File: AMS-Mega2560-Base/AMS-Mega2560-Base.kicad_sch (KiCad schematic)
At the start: 29 parts, among them J1 Conn_01x03, J2 Conn_01x03, J3 Conn_01x08, J4 Sense1, J5 Sense2, J6 AdafruitUltimateGPS, J7 Conn_02x03_Odd_Even, J8 Conn_01x03, P1 Power, P10 CONN_01X01, P11 CONN_01X01, P12 CONN_01X01, P13 CONN_01X01, P2 Analog, P3 Analog, P4 Digital, P5 PWM, P6 PWM, P7 Communication, P8 CONN_01X01, P9 CONN_01X01, T1 Conn_01x08, T2 Conn_01x08, T3 Conn_01x08, T4 Conn_01x08, T5 Conn_01x08, T6 Conn_01x08

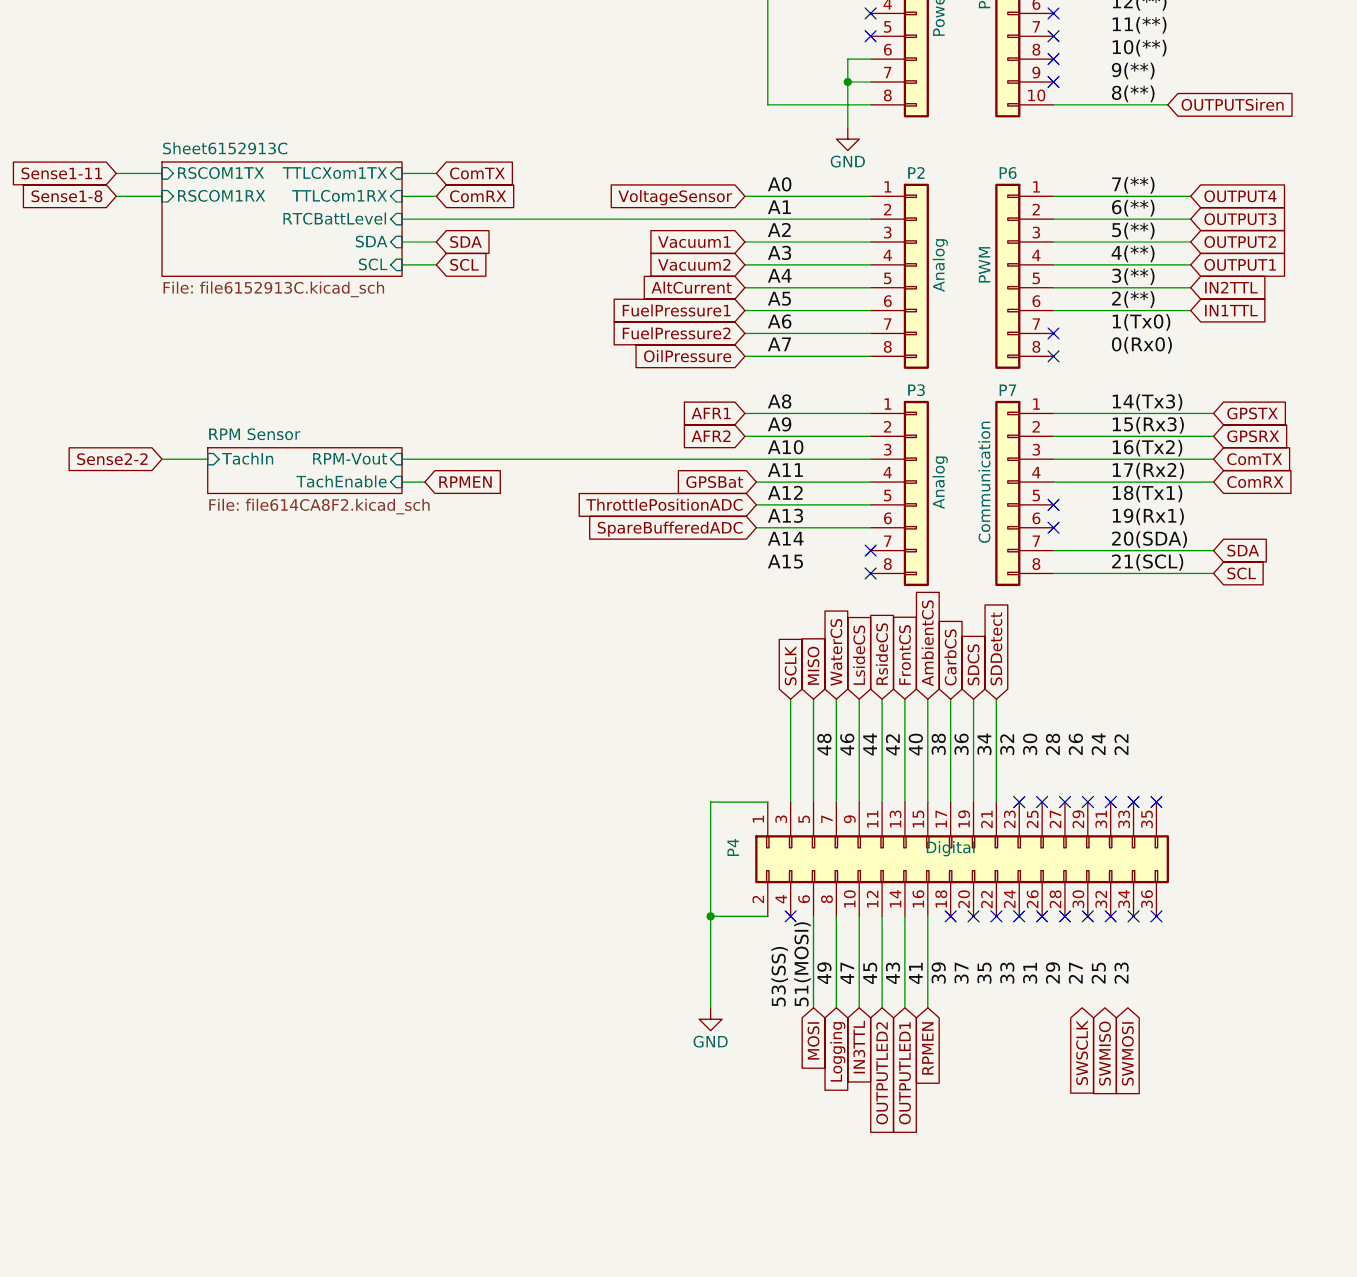
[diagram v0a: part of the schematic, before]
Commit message: working on fixing the screw ups. adding a second serial port
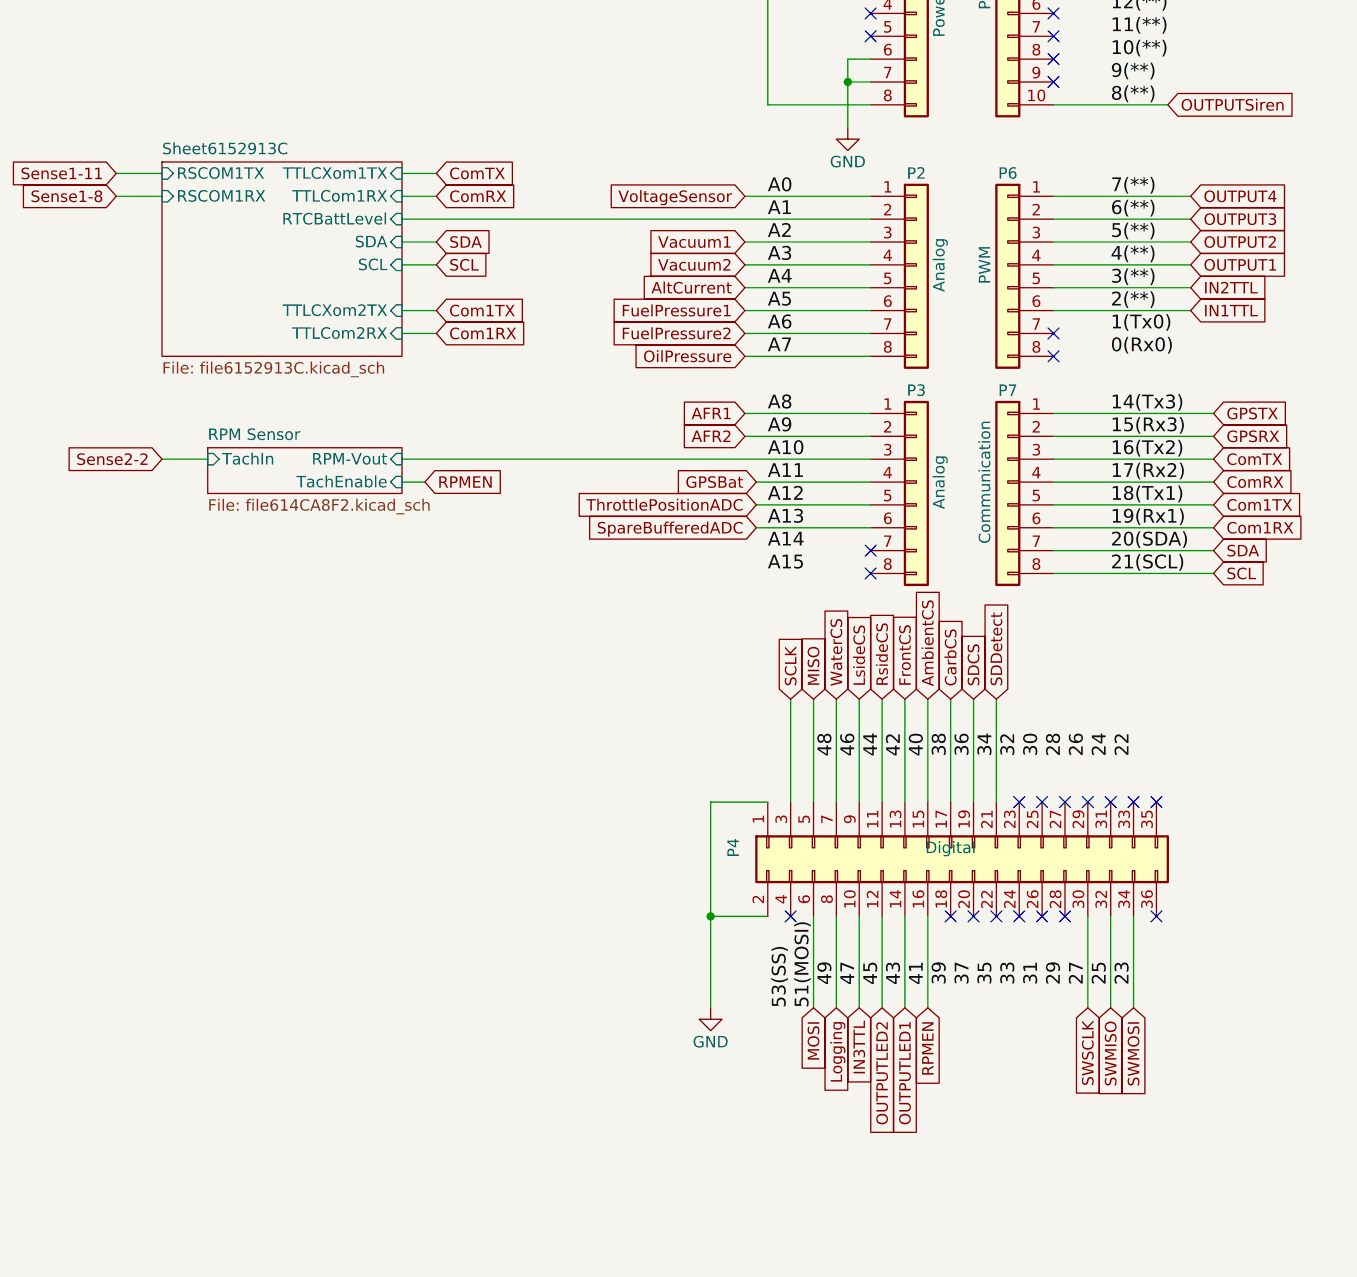
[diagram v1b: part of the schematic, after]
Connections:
- net SWMISO: now also P4.32 (Pin_32)
- net SWMOSI: now also P4.34 (Pin_34)
- net SWSCLK: now also P4.30 (Pin_30)
- net Com1TX: now reaches P7.5 (Pin_5)
- net Com1RX: now reaches P7.6 (Pin_6)
- no-connect marks 58 -> 53
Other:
- sheet Sheet6152913C ports: added TTLCXom2TX, TTLCom2RX; removed none
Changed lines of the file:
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@@
   (no_connect (at 61.595 233.045))
   (no_connect (at 355.6 101.6))
-  (no_connect (at 375.92 96.52))
-  (no_connect (at 375.92 99.06))
   (no_connect (at 364.49 142.24))
   (no_connect (at 367.03 142.24))
@@
   (no_connect (at 372.11 142.24))
   (no_connect (at 374.65 142.24))
-  (no_connect (at 382.27 142.24))
-  (no_connect (at 384.81 142.24))
   (no_connect (at 377.19 142.24))
-  (no_connect (at 379.73 142.24))
   (no_connect (at 369.57 142.24))
   (no_connect (at 375.92 49.53))
@@
     (stroke (width 0) (type default) (color 0 0 0 0))
   )
+  (wire (pts (xy 303.53 74.93) (xy 307.34 74.93))
+    (stroke (width 0) (type default) (color 0 0 0 0))
+  )
   (wire (pts (xy 367.03 118.11) (xy 367.03 129.54))
     (stroke (width 0) (type default) (color 0 0 0 0))
   )
+  (wire (pts (xy 384.81 142.24) (xy 384.81 152.4))
+    (stroke (width 0) (type default) (color 0 0 0 0))
+  )
   (wire (pts (xy 303.53 69.85) (xy 307.34 69.85))
     (stroke (width 0) (type default) (color 0 0 0 0))
@@
     (stroke (width 0) (type default) (color 0 0 0 0))
   )
+  (wire (pts (xy 379.73 142.24) (xy 379.73 152.4))
+    (stroke (width 0) (type default) (color 0 0 0 0))
+  )
   (wire (pts (xy 35.56 115.57) (xy 36.83 115.57))
     (stroke (width 0) (type default) (color 0 0 0 0))
@@
     (stroke (width 0) (type default) (color 0 0 0 0))
   )
+  (wire (pts (xy 375.92 96.52) (xy 393.7 96.52))
+    (stroke (width 0) (type default) (color 0 0 0 0))
+  )
   (wire (pts (xy 159.385 43.18) (xy 168.91 43.18))
     (stroke (width 0) (type default) (color 0 0 0 0))
@@
     (stroke (width 0) (type default) (color 0 0 0 0))
   )
+  (wire (pts (xy 382.27 142.24) (xy 382.27 152.4))
+    (stroke (width 0) (type default) (color 0 0 0 0))
+  )
   (wire (pts (xy 135.89 212.09) (xy 138.43 212.09))
     (stroke (width 0) (type default) (color 0 0 0 0))
@@
     (stroke (width 0) (type default) (color 0 0 0 0))
   )
+  (wire (pts (xy 303.53 77.47) (xy 307.34 77.47))
+    (stroke (width 0) (type default) (color 0 0 0 0))
+  )
   (polyline (pts (xy 407.67 25.4) (xy 388.62 25.4))
     (stroke (width 0) (type default) (color 0 0 0 0))
@@
   )
   (wire (pts (xy 307.34 67.31) (xy 303.53 67.31))
+    (stroke (width 0) (type default) (color 0 0 0 0))
+  )
+  (wire (pts (xy 375.92 99.06) (xy 393.7 99.06))
     (stroke (width 0) (type default) (color 0 0 0 0))
   )
@@
     )
   )
+  (global_label "Com1RX" (shape input) (at 307.34 77.47 0) (fields_autoplaced)
+    (effects (font (size 1.27 1.27)) (justify left))
+    (property "Intersheet References" "${INTERSHEET_REFS}" (id 0) (at 317.4656 77.3906 0)
+      (effects (font (size 1.27 1.27)) (justify left) hide)
+    )
+  )
   (global_label "Vacuum2" (shape input) (at 341.63 69.85 180) (fields_autoplaced)
     (effects (font (size 1.27 1.27)) (justify right))
@@
     )
   )
-  (global_label "SWMISO" (shape input) (at 381.635 152.4 270) (fields_autoplaced)
-    (effects (font (size 1.27 1.27)) (justify right))
-    (property "Intersheet References" "${INTERSHEET_REFS}" (id 0) (at 381.5556 161.9813 90)
+  (global_label "SWMISO" (shape input) (at 382.27 152.4 270) (fields_autoplaced)
+    (effects (font (size 1.27 1.27)) (justify right))
+    (property "Intersheet References" "${INTERSHEET_REFS}" (id 0) (at 382.1906 161.9813 90)
       (effects (font (size 1.27 1.27)) (justify right) hide)
     )
@@
     )
   )
-  (global_label "SWSCLK" (shape input) (at 379.095 152.4 270) (fields_autoplaced)
-    (effects (font (size 1.27 1.27)) (justify right))
-    (property "Intersheet References" "${INTERSHEET_REFS}" (id 0) (at 379.0156 162.1628 90)
+  (global_label "SWSCLK" (shape input) (at 379.73 152.4 270) (fields_autoplaced)
+    (effects (font (size 1.27 1.27)) (justify right))
+    (property "Intersheet References" "${INTERSHEET_REFS}" (id 0) (at 379.6506 162.1628 90)
       (effects (font (size 1.27 1.27)) (justify right) hide)
     )
@@
     )
   )
+  (global_label "Com1TX" (shape input) (at 393.7 96.52 0) (fields_autoplaced)
+    (effects (font (size 1.27 1.27)) (justify left))
+    (property "Intersheet References" "${INTERSHEET_REFS}" (id 0) (at 403.5232 96.4406 0)
+      (effects (font (size 1.27 1.27)) (justify left) hide)
+    )
+  )
   (global_label "Sense2-7" (shape input) (at 92.71 38.1 180) (fields_autoplaced)
     (effects (font (size 1.27 1.27)) (justify right))
@@
     )
   )
+  (global_label "Com1RX" (shape input) (at 393.7 99.06 0) (fields_autoplaced)
+    (effects (font (size 1.27 1.27)) (justify left))
+    (property "Intersheet References" "${INTERSHEET_REFS}" (id 0) (at 403.8256 98.9806 0)
+      (effects (font (size 1.27 1.27)) (justify left) hide)
+    )
+  )
   (global_label "SpareBufferedADC" (shape input) (at 342.9 99.06 180) (fields_autoplaced)
     (effects (font (size 1.27 1.27)) (justify right))
@@
     )
   )
-  (global_label "SWMOSI" (shape input) (at 384.175 152.4 270) (fields_autoplaced)
-    (effects (font (size 1.27 1.27)) (justify right))
-    (property "Intersheet References" "${INTERSHEET_REFS}" (id 0) (at 384.0956 161.9813 90)
+  (global_label "SWMOSI" (shape input) (at 384.81 152.4 270) (fields_autoplaced)
+    (effects (font (size 1.27 1.27)) (justify right))
+    (property "Intersheet References" "${INTERSHEET_REFS}" (id 0) (at 384.7306 161.9813 90)
       (effects (font (size 1.27 1.27)) (justify right) hide)
     )
@@
     (effects (font (size 1.27 1.27)) (justify left))
     (property "Intersheet References" "${INTERSHEET_REFS}" (id 0) (at 401.8904 67.2306 0)
+      (effects (font (size 1.27 1.27)) (justify left) hide)
+    )
+  )
+  (global_label "Com1TX" (shape input) (at 307.34 74.93 0) (fields_autoplaced)
+    (effects (font (size 1.27 1.27)) (justify left))
+    (property "Intersheet References" "${INTERSHEET_REFS}" (id 0) (at 317.1632 74.8506 0)
       (effects (font (size 1.27 1.27)) (justify left) hide)
     )
@@
     )
   )
-  (sheet (at 276.86 58.42) (size 26.67 12.7) (fields_autoplaced)
+  (sheet (at 276.86 58.42) (size 26.67 21.59) (fields_autoplaced)
     (stroke (width 0) (type solid) (color 0 0 0 0))
     (fill (color 0 0 0 0.0000))
@@
       (effects (font (size 1.27 1.27)) (justify left bottom))
     )
-    (property "Sheet file" "file6152913C.kicad_sch" (id 1) (at 276.86 71.7046 0)
+    (property "Sheet file" "file6152913C.kicad_sch" (id 1) (at 276.86 80.5946 0)
       (effects (font (size 1.27 1.27)) (justify left top))
     )
@@
       (effects (font (size 1.27 1.27)) (justify right))
     )
+    (pin "TTLCXom2TX" input (at 303.53 74.93 0)
+      (effects (font (size 1.27 1.27)) (justify right))
+    )
+    (pin "TTLCom2RX" input (at 303.53 77.47 0)
+      (effects (font (size 1.27 1.27)) (justify right))
+    )

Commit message: still working on the base code. updating some of the HW stuff
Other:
- sheet Sheet6152913C ports: added RSCOM2RX, RSCOM2TX; removed none
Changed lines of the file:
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@@
       (effects (font (size 1.27 1.27)) (justify right))
+    )
+    (pin "RSCOM2RX" input (at 276.86 68.58 180)
+      (effects (font (size 1.27 1.27)) (justify left))
+    )
+    (pin "RSCOM2TX" input (at 276.86 71.12 180)
+      (effects (font (size 1.27 1.27)) (justify left))
     )
   )

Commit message: updating this for the merge.
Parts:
- removed RV4: 500k, Potentiometer_THT:Potentiometer_Bourns_3296W_Vertical, symbol Device:R_POT_US
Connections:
- net GPSRX: now also P7.1 (Pin_1); no longer P7.2 (Pin_2)
- net GPSTX: now also P7.2 (Pin_2); no longer P7.1 (Pin_1)
- net Com1RX: no longer names the net of P7.6 (Pin_6)
- net Com1TX: no longer names the net of P7.5 (Pin_5)
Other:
- sheet Sheet6152913C ports: added none; removed RSCOM2RX, RSCOM2TX, TTLCXom2TX, TTLCom2RX

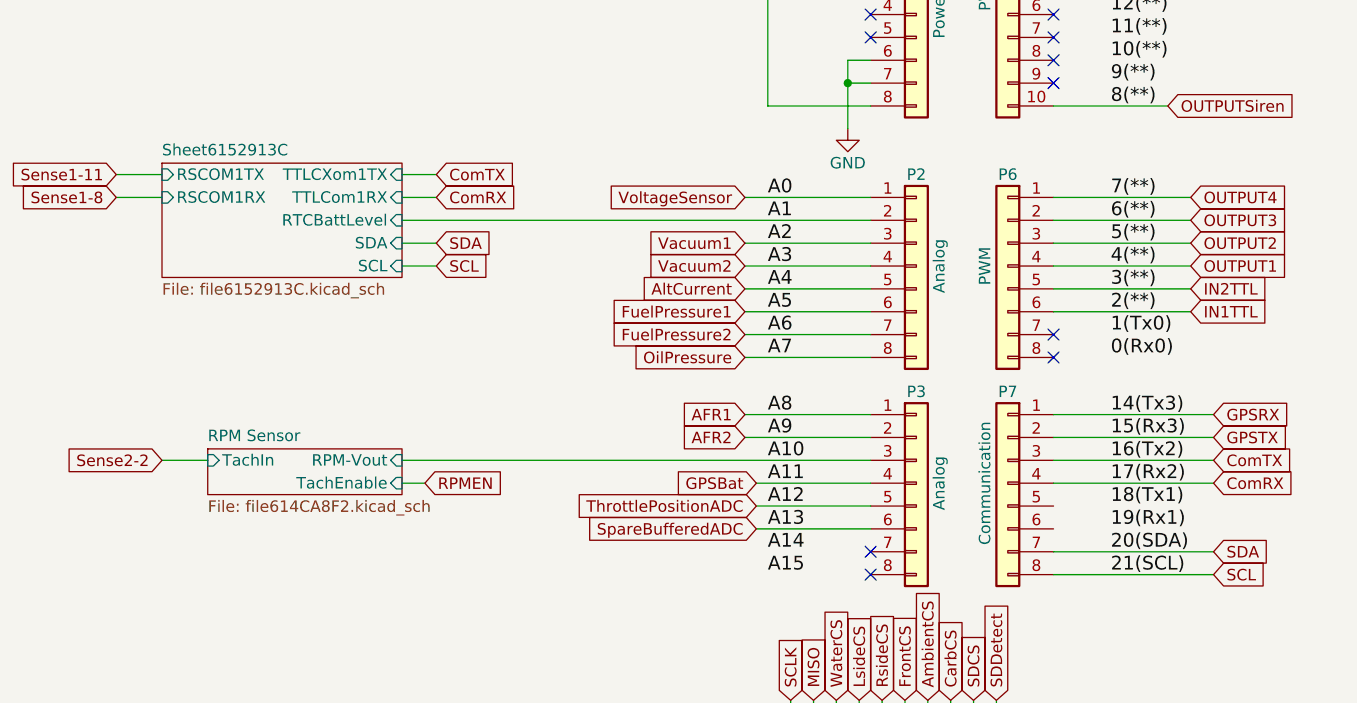
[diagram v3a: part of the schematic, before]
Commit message: wip for adding second rs232 port. needs to have the other end added to an output pin/port
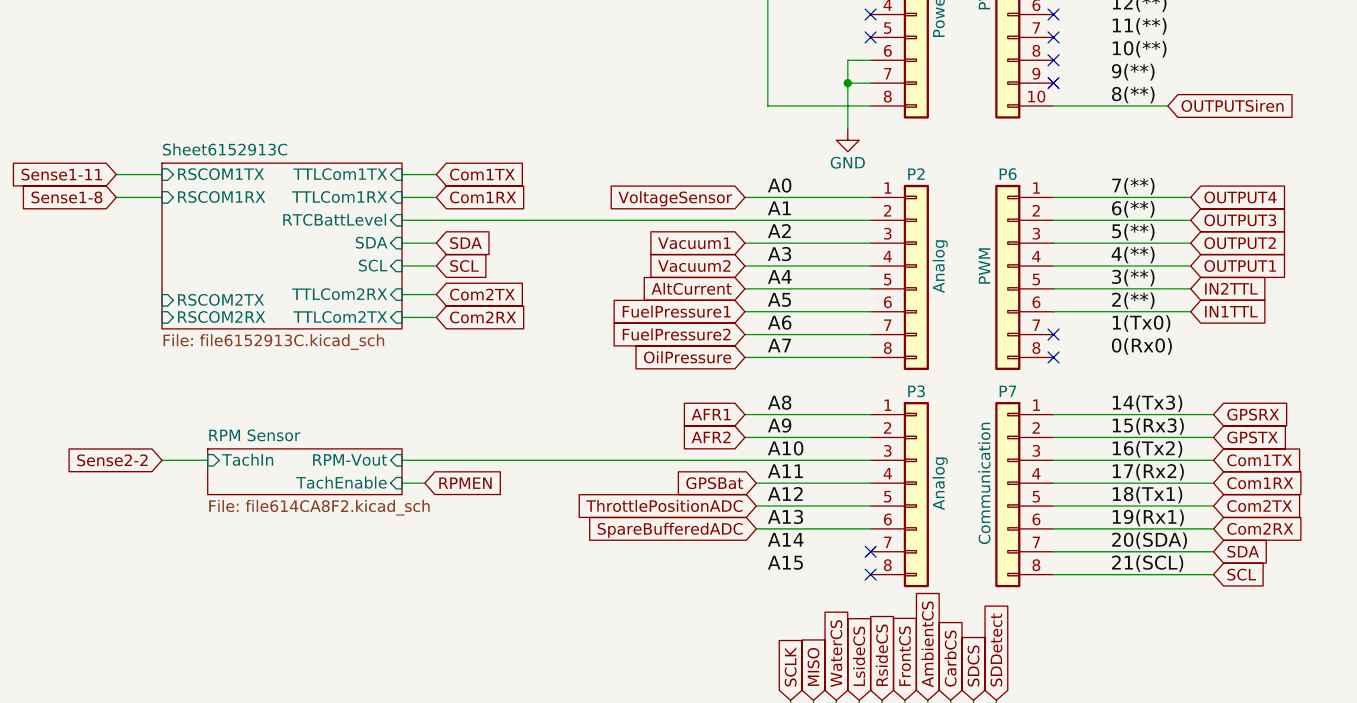
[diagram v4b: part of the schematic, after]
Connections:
- net Com2TX: now reaches P7.5 (Pin_5)
- net Com2RX: now reaches P7.6 (Pin_6)
- net ComRX renamed Com1RX
- net ComTX renamed Com1TX
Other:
- sheet Sheet6152913C ports: added RSCOM2RX, RSCOM2TX, TTLCom1TX, TTLCom2RX, TTLCom2TX; removed TTLCXom1TX
